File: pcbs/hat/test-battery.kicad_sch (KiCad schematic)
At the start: 21 parts, among them J2 XT60, Q1 Q_NMOS_DGS, Q2 Q_NMOS_DGS, U1 INA181A4IDBVR, U2 TP5000_Breakout_Akaddy

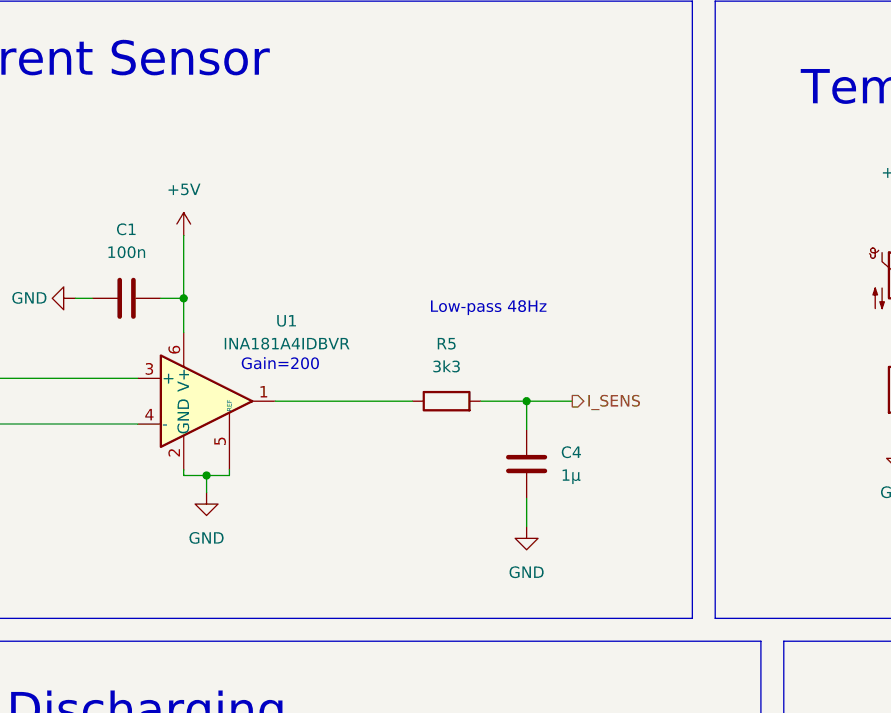
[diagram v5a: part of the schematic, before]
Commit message: fix the current sensor
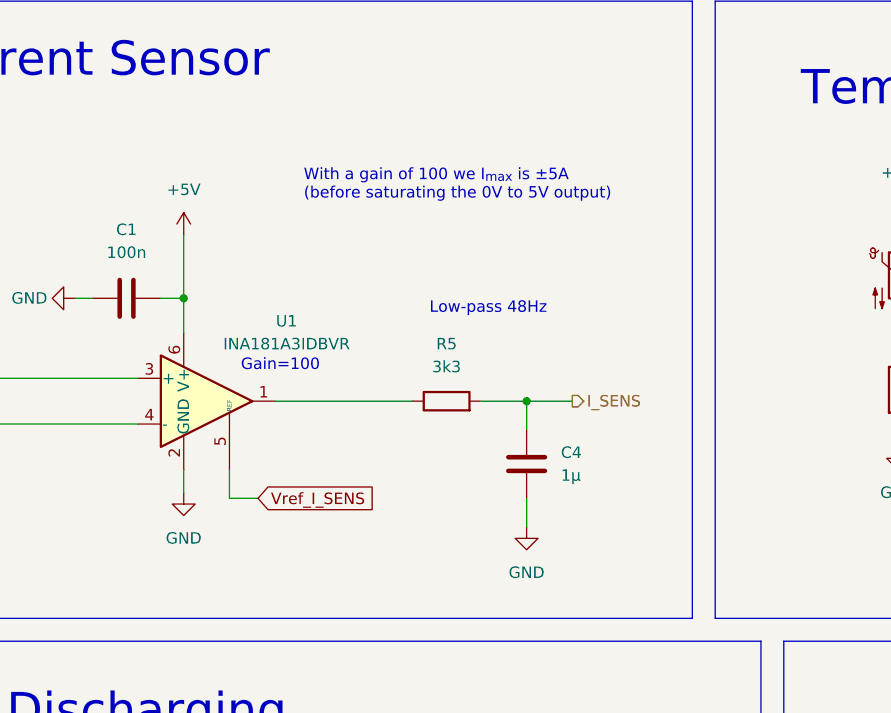
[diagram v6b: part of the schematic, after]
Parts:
- U1: value INA181A4IDBVR -> INA181A3IDBVR
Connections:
- net GND: no longer U1.5 (REF)
- new net Vref_I_SENS: U1.5 (REF)
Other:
- note added: "Gain=100"
- note added: "With a gain of 100 we I_{max} is ±5A (before saturating the 0V to 5V output)"
- note removed: "Gain=200"
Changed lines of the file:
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@@
   (junction (at 167.64 49.53) (diameter 0) (color 0 0 0 0)
-  )
-  (junction (at 90.805 65.405) (diameter 0) (color 0 0 0 0)
   )
   (junction (at 102.87 148.59) (diameter 0) (color 0 0 0 0)
@@
     (stroke (width 0) (type default) (color 0 0 0 0))
   )
-  (wire (pts (xy 93.345 65.405) (xy 93.345 64.77))
-    (stroke (width 0) (type default) (color 0 0 0 0))
-  )
   (polyline (pts (xy 12.7 12.7) (xy 144.78 12.7))
     (stroke (width 0) (type default) (color 0 0 0 0))
@@
     (stroke (width 0) (type default) (color 0 0 0 0))
   )
-  (wire (pts (xy 88.265 64.77) (xy 88.265 65.405))
-    (stroke (width 0) (type default) (color 0 0 0 0))
-  )
   (polyline (pts (xy 273.05 161.29) (xy 154.94 161.29))
     (stroke (width 0) (type default) (color 0 0 0 0))
@@
     (stroke (width 0) (type default) (color 0 0 0 0))
   )
-  (wire (pts (xy 90.805 67.31) (xy 90.805 65.405))
+  (wire (pts (xy 88.265 64.77) (xy 88.265 67.31))
     (stroke (width 0) (type default) (color 0 0 0 0))
   )
@@
     (stroke (width 0) (type default) (color 0 0 0 0))
   )
-  (wire (pts (xy 90.805 65.405) (xy 88.265 65.405))
-    (stroke (width 0) (type default) (color 0 0 0 0))
-  )
   (polyline (pts (xy 20.32 156.21) (xy 20.32 118.11))
     (stroke (width 0) (type default) (color 0 0 0 0))
@@
     (stroke (width 0) (type default) (color 0 0 0 0))
   )
+  (wire (pts (xy 93.345 64.77) (xy 93.345 67.945))
+    (stroke (width 0) (type default) (color 0 0 0 0))
+  )
   (wire (pts (xy 186.69 139.7) (xy 190.5 139.7))
     (stroke (width 0) (type default) (color 0 0 0 0))
@@
     (stroke (width 0) (type default) (color 0 0 0 0))
   )
-  (wire (pts (xy 90.805 65.405) (xy 93.345 65.405))
-    (stroke (width 0) (type default) (color 0 0 0 0))
-  )
   (wire (pts (xy 96.52 127) (xy 96.52 125.73))
     (stroke (width 0) (type default) (color 0 0 0 0))
@@
   )
   (wire (pts (xy 76.2 45.72) (xy 78.105 45.72))
+    (stroke (width 0) (type default) (color 0 0 0 0))
+  )
+  (wire (pts (xy 96.52 67.945) (xy 93.345 67.945))
     (stroke (width 0) (type default) (color 0 0 0 0))
   )
@@
     (effects (font (size 1.27 1.27)) (justify left bottom))
   )
-  (text "Gain=200" (at 94.615 53.975 0)
+  (text "Gain=100" (at 94.615 53.975 0)
     (effects (font (size 1.27 1.27)) (justify left bottom))
   )
@@
     (effects (font (size 1.27 1.27)) (justify left bottom))
   )
+  (text "With a gain of 100 we I_{max} is ±5A\n(before saturating the 0V to 5V output)"
+    (at 101.6 34.925 0)
+    (effects (font (size 1.27 1.27)) (justify left bottom))
+  )
   (text "Breakout Pictures:" (at 232.41 128.27 0)
     (effects (font (size 1.27 1.27)) (justify left bottom))
@@
   (label "VBAT" (at 219.71 111.76 180)
     (effects (font (size 1.27 1.27)) (justify right bottom))
+  )
+  (global_label "Vref_I_SENS" (shape input) (at 96.52 67.945 0) (fields_autoplaced)
+    (effects (font (size 1.27 1.27)) (justify left))
+    (property "Intersheet References" "${INTERSHEET_REFS}" (id 0) (at 110.0607 67.8656 0)
+      (effects (font (size 1.27 1.27)) (justify left) hide)
+    )
   )
   (hierarchical_label "SIG_LOAD" (shape input) (at 72.39 148.59 180)
@@
   (symbol (lib_id "power:GND") (at 90.17 163.83 0) (unit 1)
     (in_bom yes) (on_board yes) (fields_autoplaced)
-    (property "Reference" "#PWR07" (id 0) (at 90.17 170.18 0)
+    (property "Reference" "#PWR08" (id 0) (at 90.17 170.18 0)
       (effects (font (size 1.27 1.27)) hide)
     )
@@
     )
   )
-  (symbol (lib_id "power:GND") (at 90.805 67.31 0) (unit 1)
+  (symbol (lib_id "power:GND") (at 88.265 67.31 0) (unit 1)
     (in_bom yes) (on_board yes)
-    (property "Reference" "#PWR08" (id 0) (at 90.805 73.66 0)
-      (effects (font (size 1.27 1.27)) hide)
-    )
-    (property "Value" "GND" (id 1) (at 90.805 72.39 0))
-    (property "Footprint" "" (id 2) (at 90.805 67.31 0)
-      (effects (font (size 1.27 1.27)) hide)
-    )
-    (property "Datasheet" "" (id 3) (at 90.805 67.31 0)
+    (property "Reference" "#PWR07" (id 0) (at 88.265 73.66 0)
+      (effects (font (size 1.27 1.27)) hide)
+    )
+    (property "Value" "GND" (id 1) (at 88.265 72.39 0))
+    (property "Footprint" "" (id 2) (at 88.265 67.31 0)
+      (effects (font (size 1.27 1.27)) hide)
+    )
+    (property "Datasheet" "" (id 3) (at 88.265 67.31 0)
       (effects (font (size 1.27 1.27)) hide)
     )
@@
     (in_bom yes) (on_board yes)
     (property "Reference" "U1" (id 0) (at 99.695 48.26 0))
-    (property "Value" "INA181A4IDBVR" (id 1) (at 99.695 50.8 0))
+    (property "Value" "INA181A3IDBVR" (id 1) (at 99.695 50.8 0))
     (property "Footprint" "Package_TO_SOT_SMD:SOT-23-6" (id 2) (at 92.075 55.88 0)
       (effects (font (size 1.27 1.27)) hide)

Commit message: cleanup
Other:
- note added: "V_{to} < 2.5V"
- note removed: "V_{to} < 3V"
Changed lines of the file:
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@@
     (effects (font (size 1.27 1.27)) (justify left bottom))
   )
-  (text "V_{to} < 3V\n" (at 207.01 144.78 0)
+  (text "V_{to} < 2.5V\n" (at 207.01 144.78 0)
     (effects (font (size 1.27 1.27)) (justify left bottom))
   )

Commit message: few little change
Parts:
- removed #BT1: Battery, symbol Device:Battery_Cell
- removed #R1: R_{intern}, symbol Device:R
- removed C3: 220u, Capacitor_THT:CP_Radial_D6.3mm_P2.50mm, symbol Device:C_Polarized
- removed R2: 1, Resistor_THT:R_Axial_DIN0617_L17.0mm_D6.0mm_P25.40mm_Horizontal, symbol Device:R
- added C3: 0u, symbol Device:C
- C1: renamed from C2; value 100n -> 200n
- C4: value 1µ -> 15u; footprint Capacitor_SMD:C_0603_1608Metric -> Capacitor_SMD:C_0805_2012Metric
- C5: value C -> 1u
- J2: footprint Connector_AMASS:AMASS_XT60-M_1x02_P7.20mm_Vertical -> Connector_Phoenix_MSTB:PhoenixContact_MSTBA_2,5_2-G-5,08_1x02_P5.08mm_Horizontal
- R4: renamed from R5; value 3k3 -> 1k
- U1: value INA181A3IDBVR -> INA181A2IDBVR
- renumbered C1 to C2, R3 to R1, R1 to R2, R4 to R3, R7 to R5, R8 to R7
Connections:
- net GND: now also C3.2
- net T_SENS: now also C5.1
- net V_SENS: now also Q1.1 (D), C3.1
- no-connect marks 3 -> 2
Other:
- note added: "10k Resistor + 1u Capacitor ~ 16Hz Low-Pass"
- note added: "1170Hz Low-Pass"
- note added: "Gain=50"
- note added: "Low-pass 10Hz"
- note added: "Only include a footpring, just in case we decide to use it"
- note removed: "Battery"
- note removed: "Battery looks like this"
- note removed: "Can/Should we put a capacitor here to filter the signal a little?"
- note removed: "Fake Load"
- note removed: "Gain=100"
- note removed: "Low-pass 48Hz"
- note removed: "Power Rating > 5W"
- moved on the sheet: C1, C4, Q1, Q2, R1, R3, R5, R7, U2
